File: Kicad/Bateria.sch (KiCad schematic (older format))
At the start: 1 part, among them P2 BAT

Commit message: Circuito de cargador modificado. A los demás les agregué capacitor en la alimentación, pines sin conexión y cambié BATT- por GND
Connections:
- net labels added: GND
- net labels removed: -BATT
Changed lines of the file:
@@
 $EndComp
 $Comp
-L +BATT #PWR13
+L +BATT #PWR20
 U 1 1 57DDA8D2
 P 5000 3650
-F 0 "#PWR13" H 5000 3500 50  0001 C CNN
+F 0 "#PWR20" H 5000 3500 50  0001 C CNN
 F 1 "+BATT" H 5000 3790 50  0000 C CNN
 F 2 "" H 5000 3650 50  0000 C CNN
@@
 $EndComp
 $Comp
-L -BATT #PWR14
-U 1 1 57DDA938
+L GND #PWR21
+U 1 1 57FAD2FA
 P 5500 3650
-F 0 "#PWR14" H 5500 3500 50  0001 C CNN
-F 1 "-BATT" H 5500 3790 50  0000 C CNN
+F 0 "#PWR21" H 5500 3400 50  0001 C CNN
+F 1 "GND" H 5500 3500 50  0000 C CNN
 F 2 "" H 5500 3650 50  0000 C CNN
 F 3 "" H 5500 3650 50  0000 C CNN
 	1    5500 3650
-	0    1    1    0
+	1    0    0    -1
 $EndComp
 $EndSCHEMATC

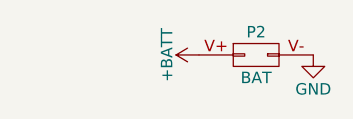
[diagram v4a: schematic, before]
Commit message: Agregado switch en esquemático
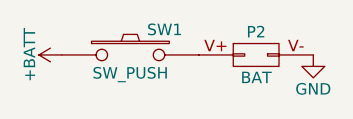
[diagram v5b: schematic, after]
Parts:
- added SW1: SW_PUSH, symbol SW_PUSH
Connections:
- net +BATT: now also SW1.1; no longer P2.V+
- new net: P2.V+, SW1.2
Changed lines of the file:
@@
 $EndComp
 $Comp
-L +BATT #PWR020
+L +BATT #PWR20
 U 1 1 57DDA8D2
-P 5000 3650
-F 0 "#PWR020" H 5000 3500 50  0001 C CNN
-F 1 "+BATT" H 5000 3790 50  0000 C CNN
-F 2 "" H 5000 3650 50  0000 C CNN
-F 3 "" H 5000 3650 50  0000 C CNN
-	1    5000 3650
+P 4400 3650
+F 0 "#PWR20" H 4400 3500 50  0001 C CNN
+F 1 "+BATT" H 4400 3790 50  0000 C CNN
+F 2 "" H 4400 3650 50  0000 C CNN
+F 3 "" H 4400 3650 50  0000 C CNN
+	1    4400 3650
 	0    -1   -1   0
 $EndComp
 $Comp
-L GND #PWR021
+L GND #PWR21
 U 1 1 57FAD2FA
 P 5500 3650
-F 0 "#PWR021" H 5500 3400 50  0001 C CNN
+F 0 "#PWR21" H 5500 3400 50  0001 C CNN
 F 1 "GND" H 5500 3500 50  0000 C CNN
 F 2 "" H 5500 3650 50  0000 C CNN
@@
 	1    0    0    -1
 $EndComp
+$Comp
+L SW_PUSH SW1
+U 1 1 583EE592
+P 4700 3650
+F 0 "SW1" H 4850 3760 50  0000 C CNN
+F 1 "SW_PUSH" H 4700 3570 50  0000 C CNN
+F 2 "" H 4700 3650 50  0000 C CNN
+F 3 "" H 4700 3650 50  0000 C CNN
+	1    4700 3650
+	1    0    0    -1
+$EndComp

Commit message: Agregados footprints de pin headers para elementos faltantes (falta USB)
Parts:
- P2, SW1: footprint (none) -> EMG:Pin_Header_Straight_1x02_Pitch2.54mm
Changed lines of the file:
@@
 F 0 "P2" H 5250 3750 50  0000 C CNN
 F 1 "BAT" H 5250 3550 50  0000 C CNN
-F 2 "" H 5250 2450 50  0001 C CNN
+F 2 "EMG:Pin_Header_Straight_1x02_Pitch2.54mm" H 5250 2450 50  0001 C CNN
 F 3 "" H 5250 2450 50  0000 C CNN
 	1    5250 3650
@@
 $EndComp
 $Comp
-L +BATT #PWR21
+L +BATT #PWR021
 U 1 1 57DDA8D2
 P 4400 3650
-F 0 "#PWR21" H 4400 3500 50  0001 C CNN
+F 0 "#PWR021" H 4400 3500 50  0001 C CNN
 F 1 "+BATT" H 4400 3790 50  0000 C CNN
 F 2 "" H 4400 3650 50  0000 C CNN
@@
 $EndComp
 $Comp
-L GND #PWR22
+L GND #PWR022
 U 1 1 57FAD2FA
 P 5500 3650
-F 0 "#PWR22" H 5500 3400 50  0001 C CNN
+F 0 "#PWR022" H 5500 3400 50  0001 C CNN
 F 1 "GND" H 5500 3500 50  0000 C CNN
 F 2 "" H 5500 3650 50  0000 C CNN
@@
 F 0 "SW1" H 4850 3760 50  0000 C CNN
 F 1 "SW_PUSH" H 4700 3570 50  0000 C CNN
-F 2 "" H 4700 3650 50  0000 C CNN
+F 2 "EMG:Pin_Header_Straight_1x02_Pitch2.54mm" H 4700 3650 50  0001 C CNN
 F 3 "" H 4700 3650 50  0000 C CNN
 	1    4700 3650

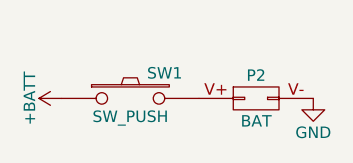
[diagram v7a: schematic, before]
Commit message: Se inició con el Pcb. Se eliminó el capacitor del socket del nrf. Se cambió el conector de la bat.
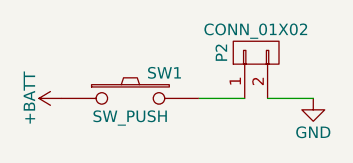
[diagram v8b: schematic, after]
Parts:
- removed P2: BAT, EMG:Pin_Header_Straight_1x02_Pitch2.54mm, symbol BAT
- added P2: CONN_01X02, EMG:Pin_Header_Straight_1x02_Pitch2.54mm, symbol CONN_01X02
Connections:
- net GND: now also P2.2 (P2)
- net at SW1.2: now also P2.1 (P1)
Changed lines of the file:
@@
 $EndDescr
-$Comp
-L BAT P2
-U 1 1 57DDA8B8
-P 5250 3650
-F 0 "P2" H 5250 3750 50  0000 C CNN
-F 1 "BAT" H 5250 3550 50  0000 C CNN
-F 2 "EMG:Pin_Header_Straight_1x02_Pitch2.54mm" H 5250 2450 50  0001 C CNN
-F 3 "" H 5250 2450 50  0000 C CNN
-	1    5250 3650
-	1    0    0    -1
-$EndComp
 $Comp
 L +BATT #PWR021
@@
 	1    0    0    -1
 $EndComp
+$Comp
+L CONN_01X02 P2
+U 1 1 58BC865C
+P 5250 3450
+F 0 "P2" H 5250 3600 50  0000 C CNN
+F 1 "CONN_01X02" V 5350 3450 50  0000 C CNN
+F 2 "EMG:Pin_Header_Straight_1x02_Pitch2.54mm" H 5250 3450 50  0001 C CNN
+F 3 "" H 5250 3450 50  0000 C CNN
+	1    5250 3450
+	0    -1   -1   0
+$EndComp
+Wire Wire Line
+	5500 3650 5300 3650
+Wire Wire Line
+	5000 3650 5200 3650
 $EndSCHEMATC
